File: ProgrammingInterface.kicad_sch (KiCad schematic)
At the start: 1 part, among them J1 TC2030

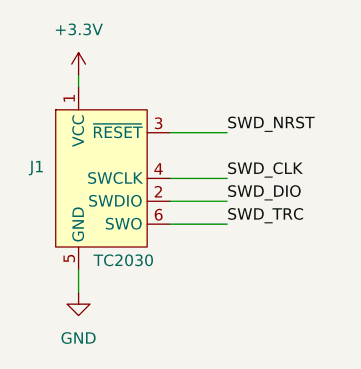
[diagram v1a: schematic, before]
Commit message: fixed some nets
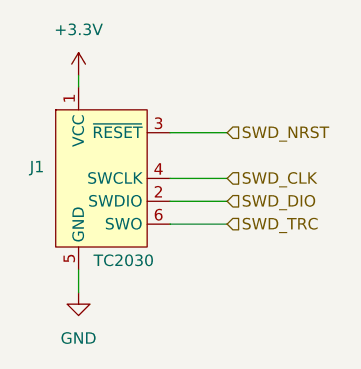
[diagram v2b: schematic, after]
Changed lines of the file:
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@@
 		)
 	)
-	(label "SWD_NRST"
+	(hierarchical_label "SWD_CLK"
+		(shape input)
+		(at 154.94 107.95 0)
+		(effects
+			(font
+				(size 1.27 1.27)
+			)
+			(justify left)
+		)
+	)
+	(hierarchical_label "SWD_TRC"
+		(shape input)
+		(at 154.94 113.03 0)
+		(effects
+			(font
+				(size 1.27 1.27)
+			)
+			(justify left)
+		)
+	)
+	(hierarchical_label "SWD_NRST"
+		(shape input)
 		(at 154.94 102.87 0)
 		(effects
@@
 				(size 1.27 1.27)
 			)
-			(justify left bottom)
+			(justify left)
 		)
 	)
-	(label "SWD_CLK"
-		(at 154.94 107.95 0)
-		(effects
-			(font
-				(size 1.27 1.27)
-			)
-			(justify left bottom)
-		)
-	)
-	(label "SWD_DIO"
+	(hierarchical_label "SWD_DIO"
+		(shape input)
 		(at 154.94 110.49 0)
 		(effects
@@
 				(size 1.27 1.27)
 			)
-			(justify left bottom)
+			(justify left)
 		)
 	)
-	(label "SWD_TRC"
-		(at 154.94 113.03 0)
-		(effects
-			(font
-				(size 1.27 1.27)
-			)
-			(justify left bottom)
-		)
-	)
